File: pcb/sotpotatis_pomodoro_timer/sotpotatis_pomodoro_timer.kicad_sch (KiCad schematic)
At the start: 40 parts, among them J1 PWR_IN, SW1 RIGHT_BTN, SW2 PRESET_1_BTN, SW3 PRESET_2_BTN, SW4 PRESET_3_BTN, SW5 LEFT_BTN, SW6 PWR_SWITCH, U1 ATtiny84A-P

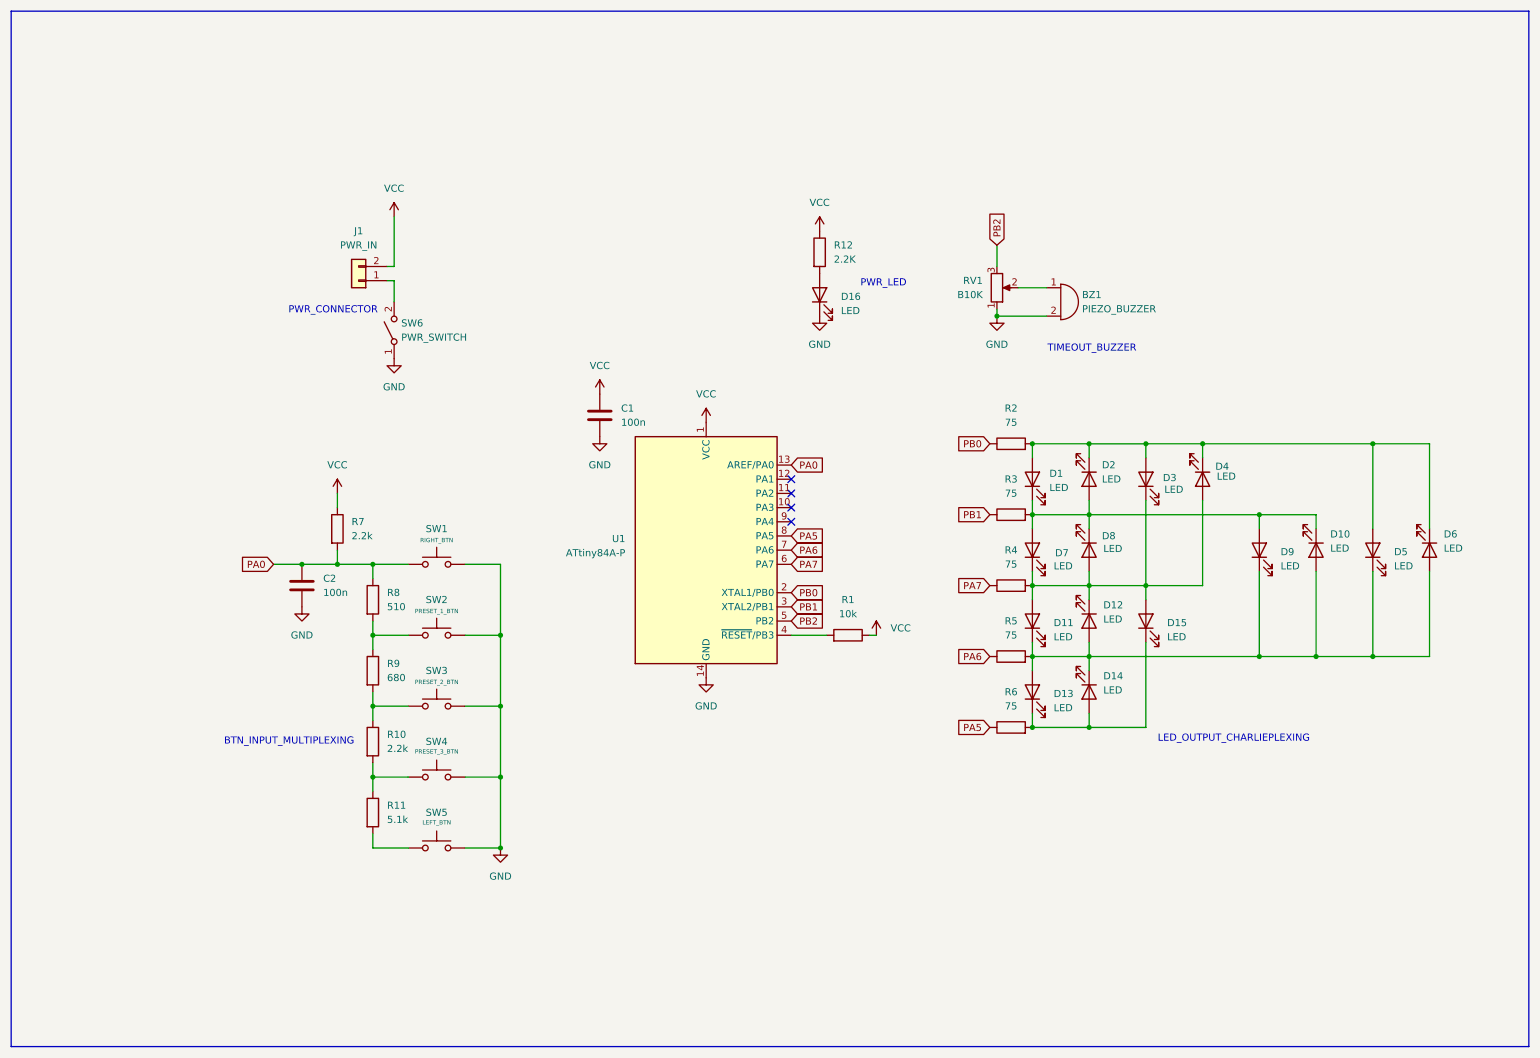
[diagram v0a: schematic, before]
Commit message: add: Update schematic according to online feedback (v0.2)
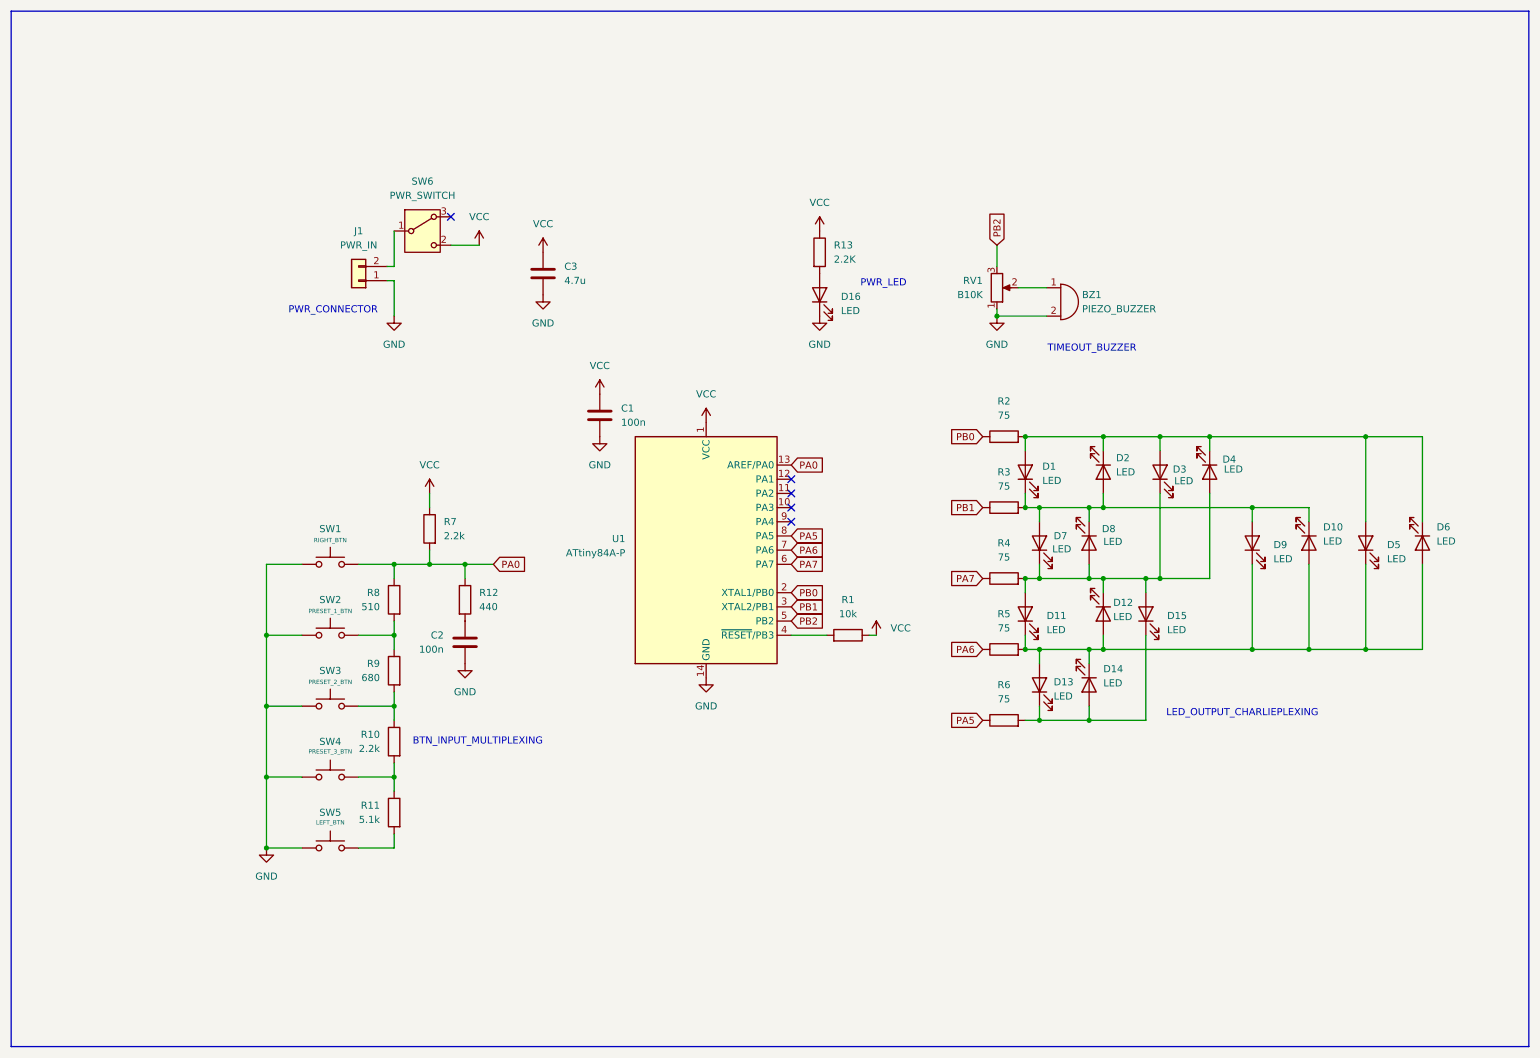
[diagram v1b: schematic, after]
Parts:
- removed SW6: PWR_SWITCH, Button_Switch_THT:SW_Slide-03_Wuerth-WS-SLTV_10x2.5x6.4_P2.54mm, symbol Switch:SW_SPST
- added C3: 4.7u, Connector_PinSocket_2.54mm:PinSocket_1x02_P2.54mm_Vertical, symbol Device:C
- added R12: 440, Connector_PinSocket_2.54mm:PinSocket_1x02_P2.54mm_Vertical, symbol Device:R
- added SW6: PWR_SWITCH, Button_Switch_THT:SW_Slide-03_Wuerth-WS-SLTV_10x2.5x6.4_P2.54mm, symbol Switch:SW_Wuerth_450301014042
- renumbered R12 to R13
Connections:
- net GND: now also J1.1 (Pin_1), C3.2
- net PA0: now also R12.1; no longer C2.1
- net VCC: now also C3.1, SW6.2 (C); no longer J1.2 (Pin_2)
- new net: J1.2 (Pin_2), SW6.1 (B)
- new net: C2.1, R12.2
- no-connect marks 4 -> 5
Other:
- moved on the sheet: C2, D1, D10, D11, D12, D13, D14, D15, D2, D3, D4, D5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

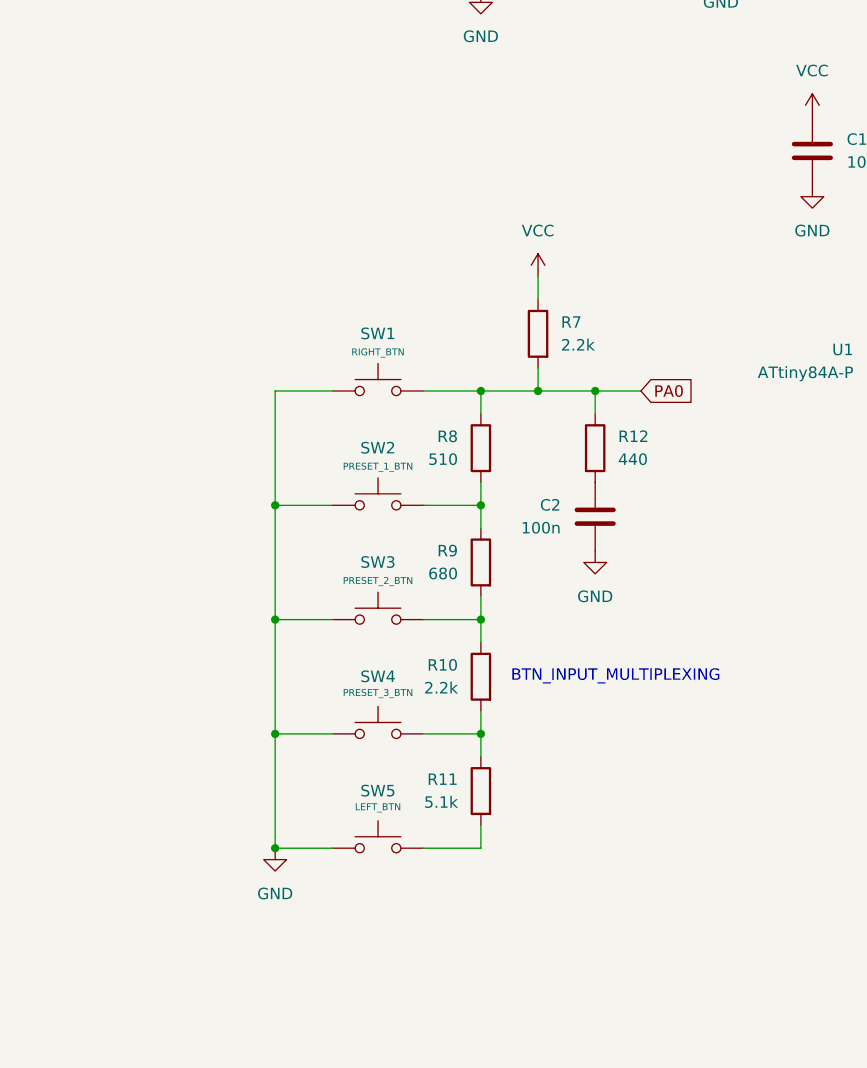
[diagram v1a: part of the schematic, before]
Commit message: add: Current-limiting resistor to PCB (v0.2)
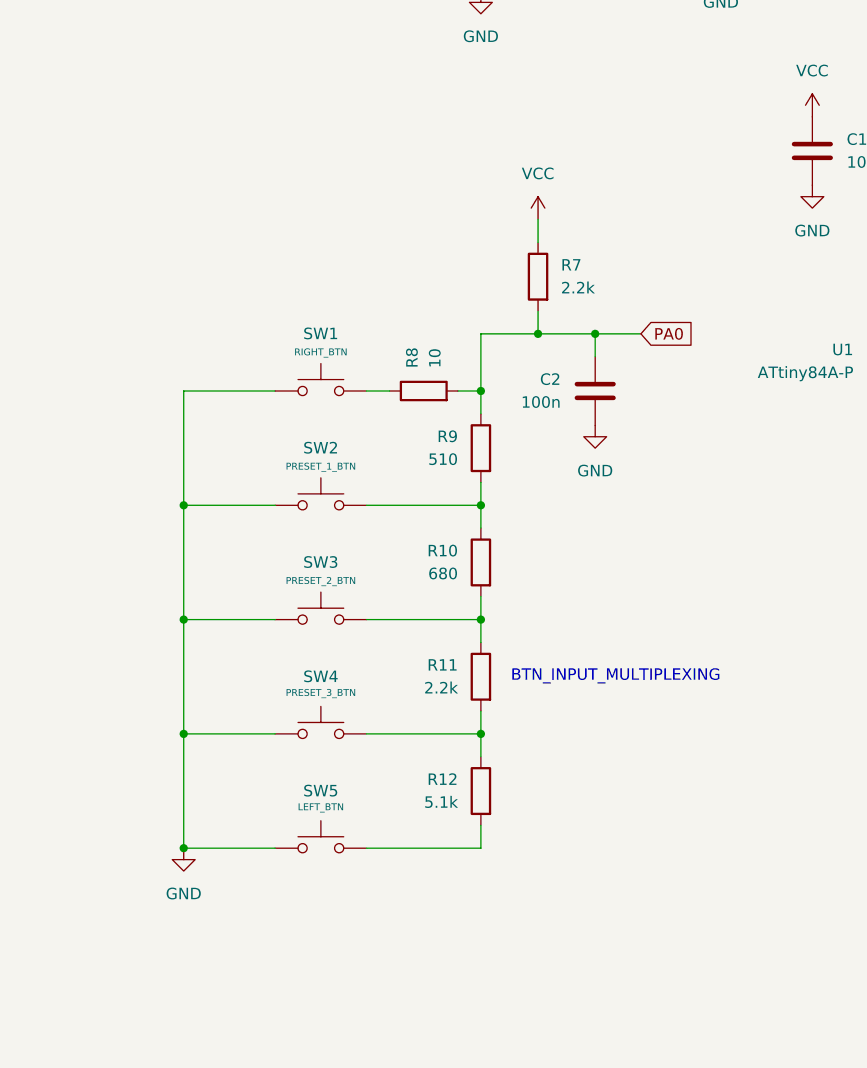
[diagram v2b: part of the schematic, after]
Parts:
- removed R12: 440, Connector_PinSocket_2.54mm:PinSocket_1x02_P2.54mm_Vertical, symbol Device:R
- added R8: 10, Connector_PinSocket_2.54mm:PinSocket_1x02_P2.54mm_Vertical, symbol Device:R
- renumbered R9 to R10, R10 to R11, R11 to R12, R8 to R9
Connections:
- net PA0: now also C2.1, R8.2; no longer SW1.1
- new net: R8.1, SW1.1
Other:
- moved on the sheet: C2, R7, SW1, SW2, SW3, SW4, SW5

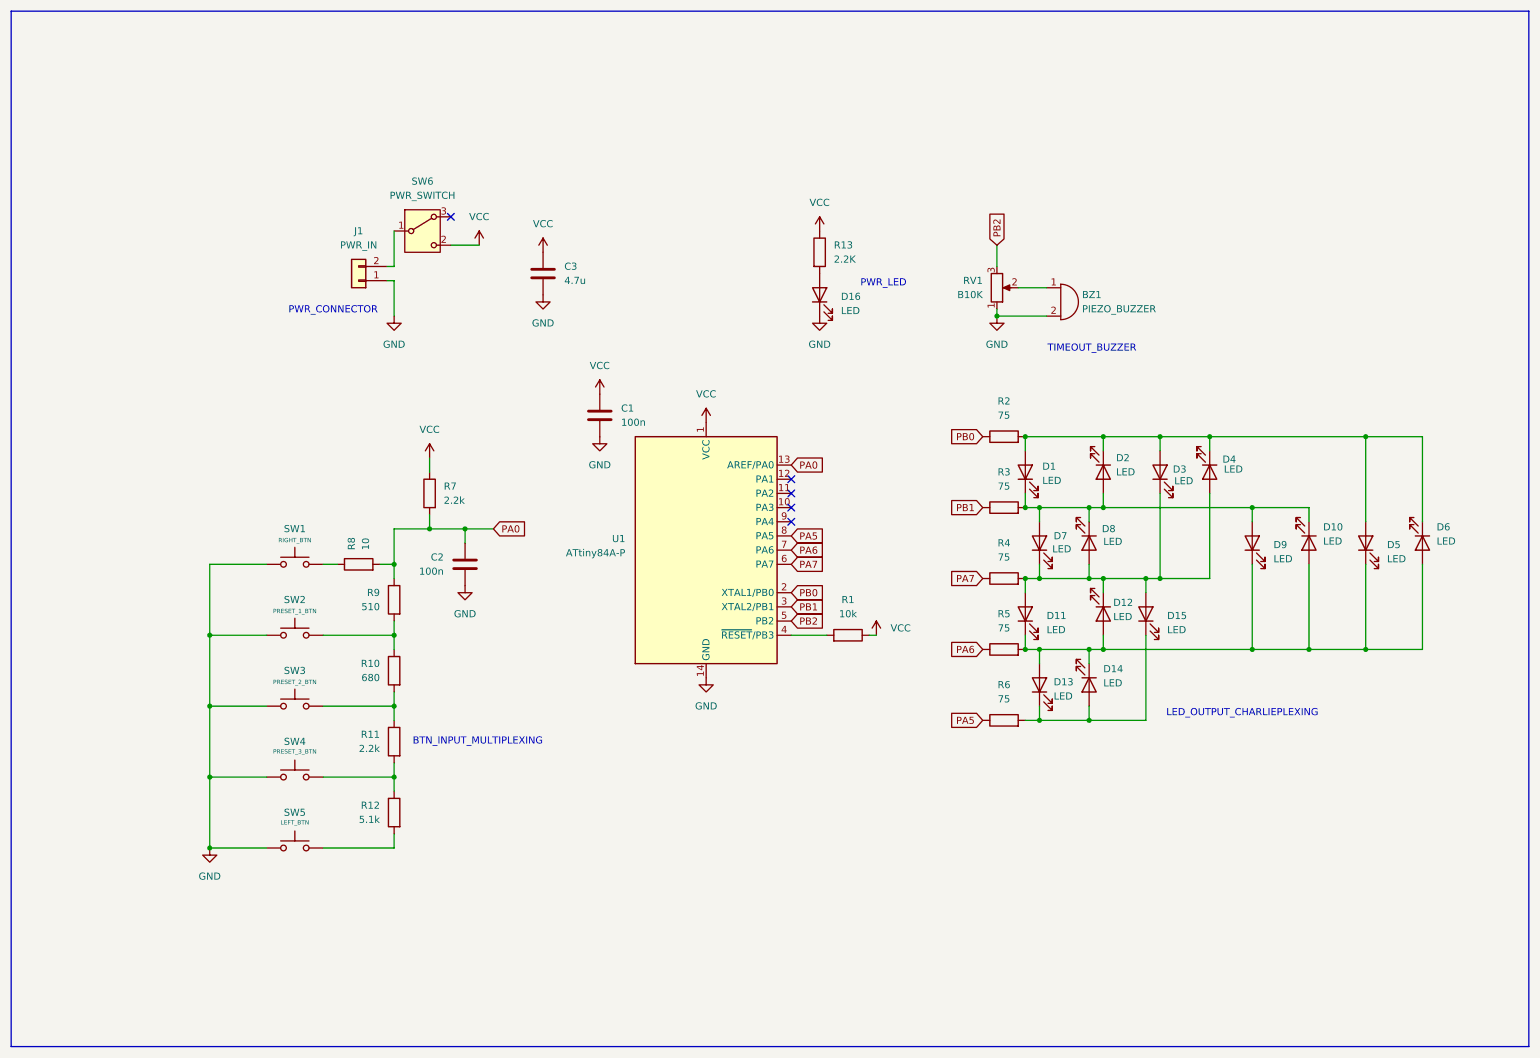
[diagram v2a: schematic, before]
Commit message: add: USB-C power input (schematics rev 0.3)
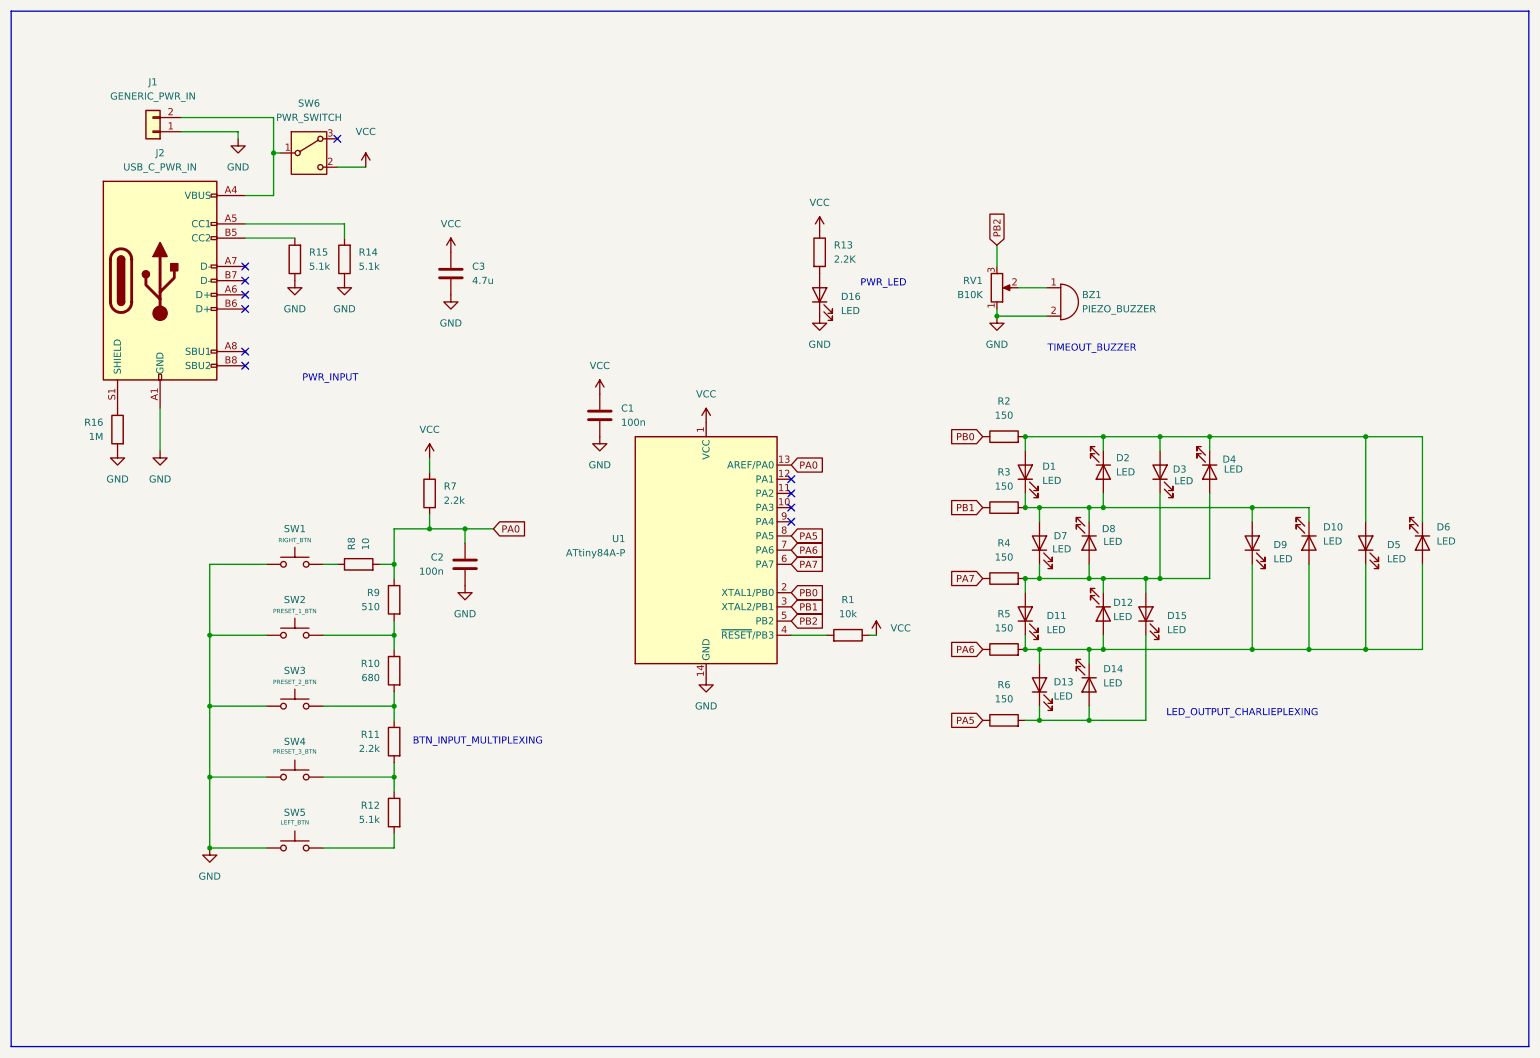
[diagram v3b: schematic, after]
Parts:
- added J2: USB_C_PWR_IN, Connector_USB:USB_C_Receptacle_HRO_TYPE-C-31-M-12, symbol Connector:USB_C_Receptacle_USB2.0_16P
- added R14, R15: 5.1k, Connector_PinSocket_2.54mm:PinSocket_1x02_P2.54mm_Vertical, symbol Device:R
- added R16: 1M, Connector_PinSocket_2.54mm:PinSocket_1x02_P2.54mm_Vertical, symbol Device:R
- J1: value PWR_IN -> GENERIC_PWR_IN
- R2, R3, R4, R5, R6: value 75 -> 150
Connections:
- net GND: now also J2.A1 (GND), J2.A12 (GND), J2.B1 (GND), J2.B12 (GND), R14.1, R15.1, R16.2
- net at J1.2 (Pin_2), SW6.1 (B): now also J2.A4 (VBUS), J2.A9 (VBUS), J2.B4 (VBUS), J2.B9 (VBUS)
- new net: J2.A5 (CC1), R14.2
- new net: J2.S1 (SHIELD), R16.1
- new net: J2.B5 (CC2), R15.2
- no-connect marks 5 -> 11
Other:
- note added: "PWR_INPUT"
- note removed: "PWR_CONNECTOR"
- moved on the sheet: C3, SW6
